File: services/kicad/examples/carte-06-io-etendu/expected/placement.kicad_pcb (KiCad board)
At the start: 2 copper layers, 47.4 x 36.3 mm, 35 parts, among them J1 IN_5V, J10 IO0, J11 IO1, J2 SWD, U1 STM32F103C8T6, U2 AMS1117-3.3

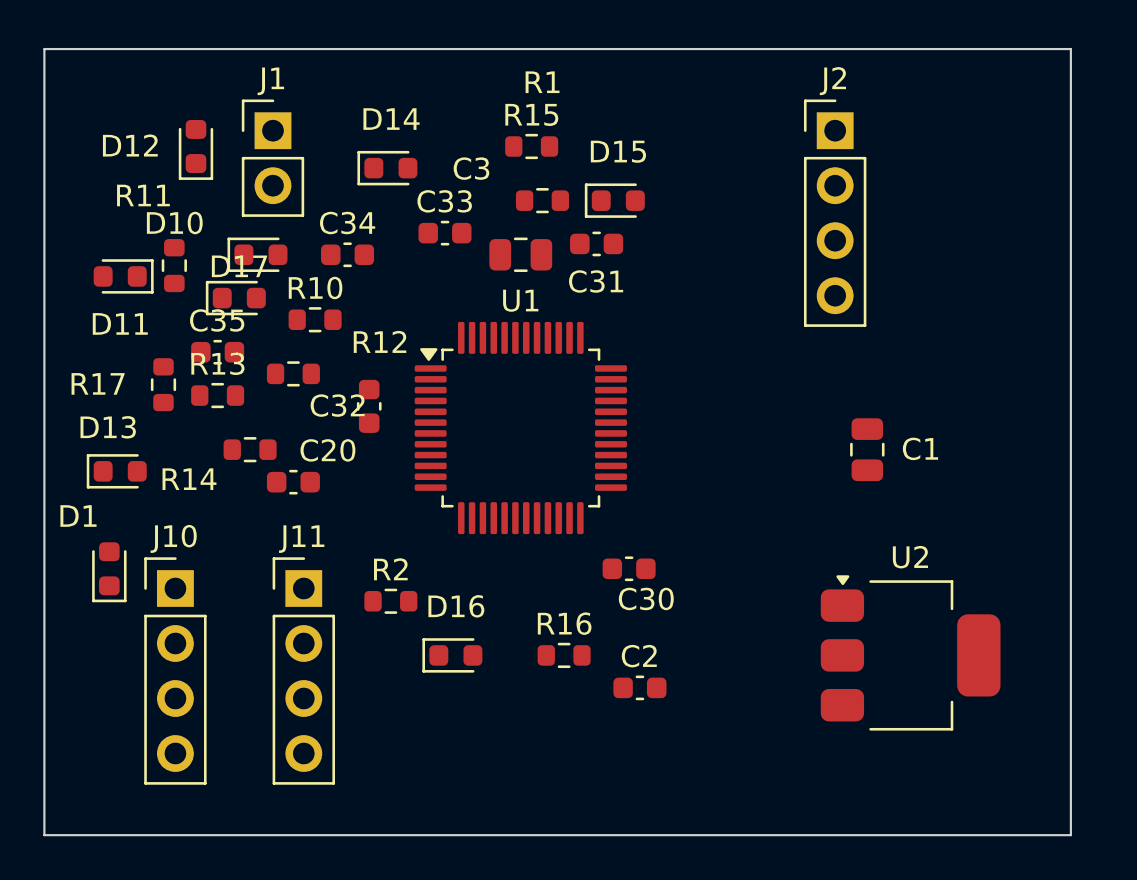
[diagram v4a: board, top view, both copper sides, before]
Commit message: fix(banc): le banc route comme la production — plafond 8, budget du client
D-2026-09-24-f. run_pipeline.py prenait 2 couches et 1800 s par défaut, et
carte-07 écrivait 2 en dur : dix cartes sur quinze ne pouvaient jamais
escalader, et la règle « toute connexion manquante fait monter » était
inerte dans le banc. Mesuré sur carte-07 : 97 %, seule la masse manquante,
« le palier suivant sera tenté »… puis retour à 2 couches.

Plafond par défaut 8 (client Pro Max), budget min(600 + 300 x plafond, 3600)
comme routingSearchBudgetS côté client. En production, rien ne change : le
plafond reste celui du plan.

Livraisons du jour, toutes vérifiées par kicad-cli et contre le schéma
(0 erreur bloquante, 0 connexion manquante, 0 court-circuit) :
carte-04, 05, 06, 08 (campagne de l'après-midi) et carte-09, 10 (4 couches).
Les boards versionnés de ces cartes court-circuitaient des nets du schéma.

Correction de ma propre erreur dans la doc : carte-07 n'avait jamais
escaladé ; les lignes « palier 4 et 6 » du journal étaient celles de
carte-08, démarrée la même minute.

Co-Authored-By: Claude Opus 5.5 <noreply@anthropic.com>
Claude-Session: https://claude.ai/code/session_01TnMqm4La2CxQHHB5K8aSSV
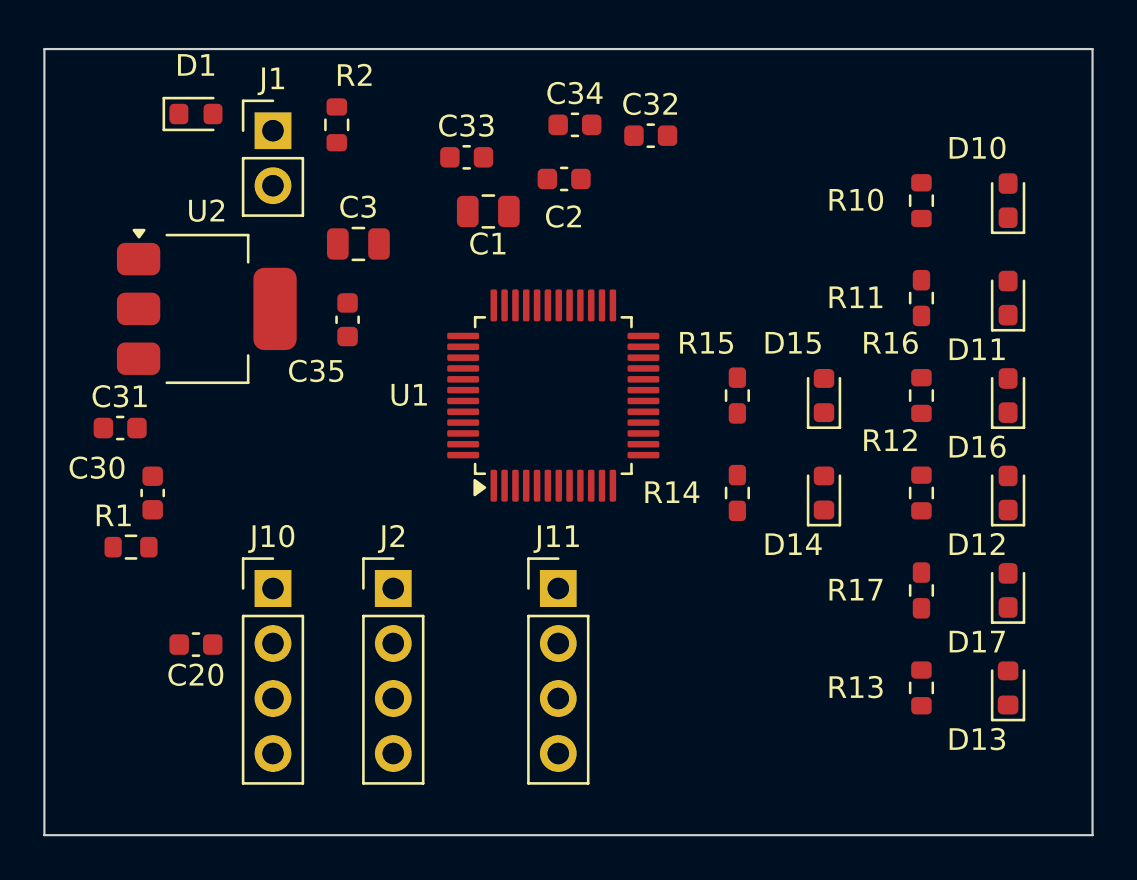
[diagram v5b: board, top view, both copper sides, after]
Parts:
- moved D13 42.2 mm to (153.0, 104.5), turned to 90 degrees
- moved D11 41.0 mm to (153.0, 86.5), turned to 90 degrees
- moved D12 40.8 mm to (153.0, 95.5)
- moved D17 38.0 mm to (153.0, 100.0), turned to 90 degrees
- moved R17 36.3 mm to (149.0, 100.0)
- moved U2 36.2 mm to (116.0, 87.0)
- moved R13 35.2 mm to (149.0, 104.5), turned to 90 degrees
- moved D10 34.6 mm to (153.0, 82.0), turned to 90 degrees
- moved R11 34.5 mm to (149.0, 86.5)
- moved R12 29.5 mm to (149.0, 95.5), turned to 90 degrees
- moved J2 29.4 mm to (124.6, 99.9)
- moved R10 28.5 mm to (149.0, 82.0), turned to 90 degrees
- moved D16 28.2 mm to (153.0, 91.0), turned to 90 degrees
- moved D14 25.0 mm to (144.5, 95.5), turned to 90 degrees
- moved R1 24.8 mm to (112.5, 98.0)
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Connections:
- U1 pad 36: PWR_FLAG -> +3V3
- U1 pad 48: PWR_FLAG -> +3V3
- U1 pad 9: PWR_FLAG -> IO_L5
- U2 pad 3: PWR_FLAG -> VIN
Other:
- board size 47.4 x 36.3 mm -> 48.4 x 36.3 mm
